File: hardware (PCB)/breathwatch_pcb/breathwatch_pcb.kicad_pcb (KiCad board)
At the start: 2 copper layers, 41.5 x 40.5 mm, 8 parts, among them J1 Conn_01x08_Socket, J2 Conn_01x08_Socket, J4 Conn_01x08_Socket, J5 USB_C_Receptacle_PowerOnly_6P, Q1 AO3401A, SW1 SW_Push

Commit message: changed a bit
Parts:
- R1, R2: footprint Resistor_THT:R_Axial_DIN0207_L6.3mm_D2.5mm_P7.62mm_Horizontal -> Resistor_SMD:R_0603_1608Metric
- moved R2 7.24 mm to (98.5, 68.4)
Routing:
- net Net-(J4-Pin_2): track 22.4 -> 30.0 mm
- net Net-(J2-Pin_2): track 10.6 -> 17.4 mm
- net Net-(J1-Pin_4): track 20.8 -> 27.3 mm
- net GND: track 67.6 -> 70.5 mm
- net Net-(Q1-G): track 14.7 -> 12.8 mm
- net Net-(J1-Pin_3): track 27.9 -> 26.3 mm
- net Net-(J1-Pin_8): track 41.2 -> 42.2 mm
- net Net-(J2-Pin_1): track 15.9 -> 16.9 mm

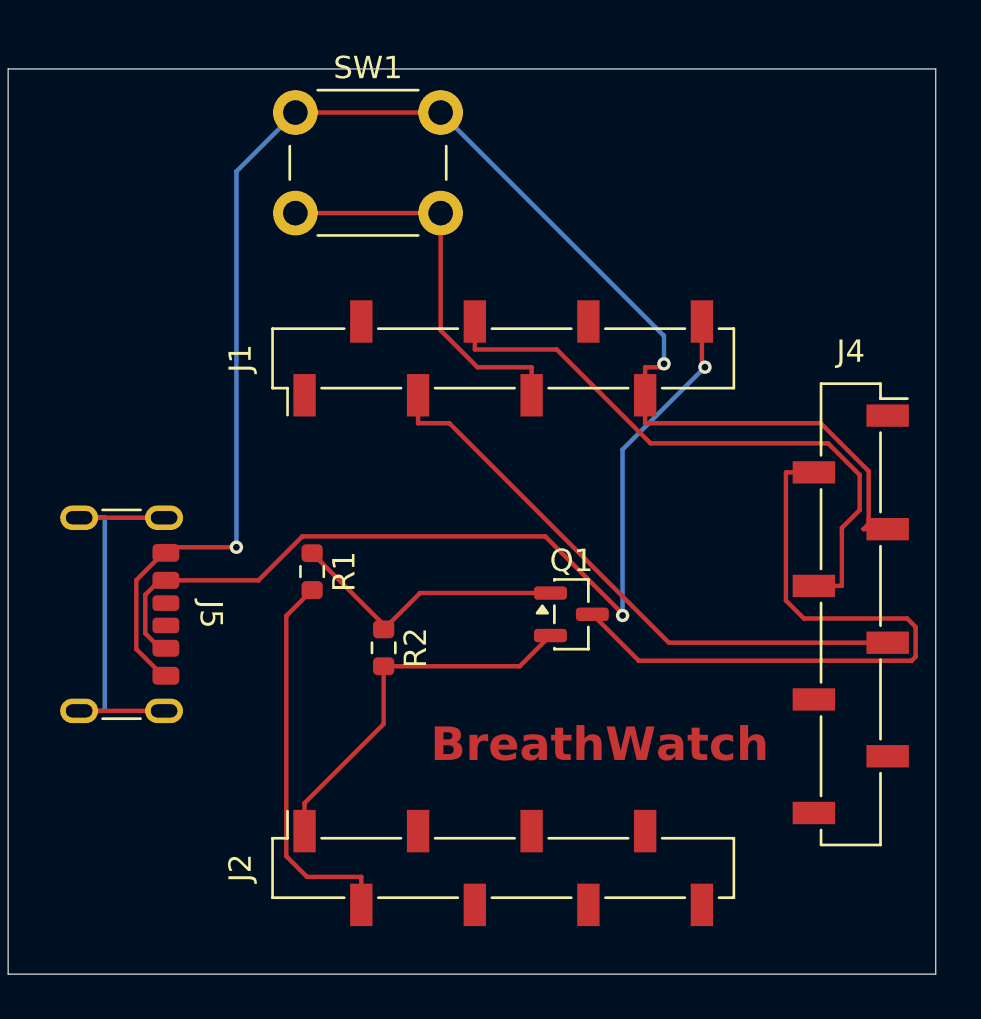
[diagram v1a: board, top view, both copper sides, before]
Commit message: added sensor reading + writing, changed a bit (PCB)
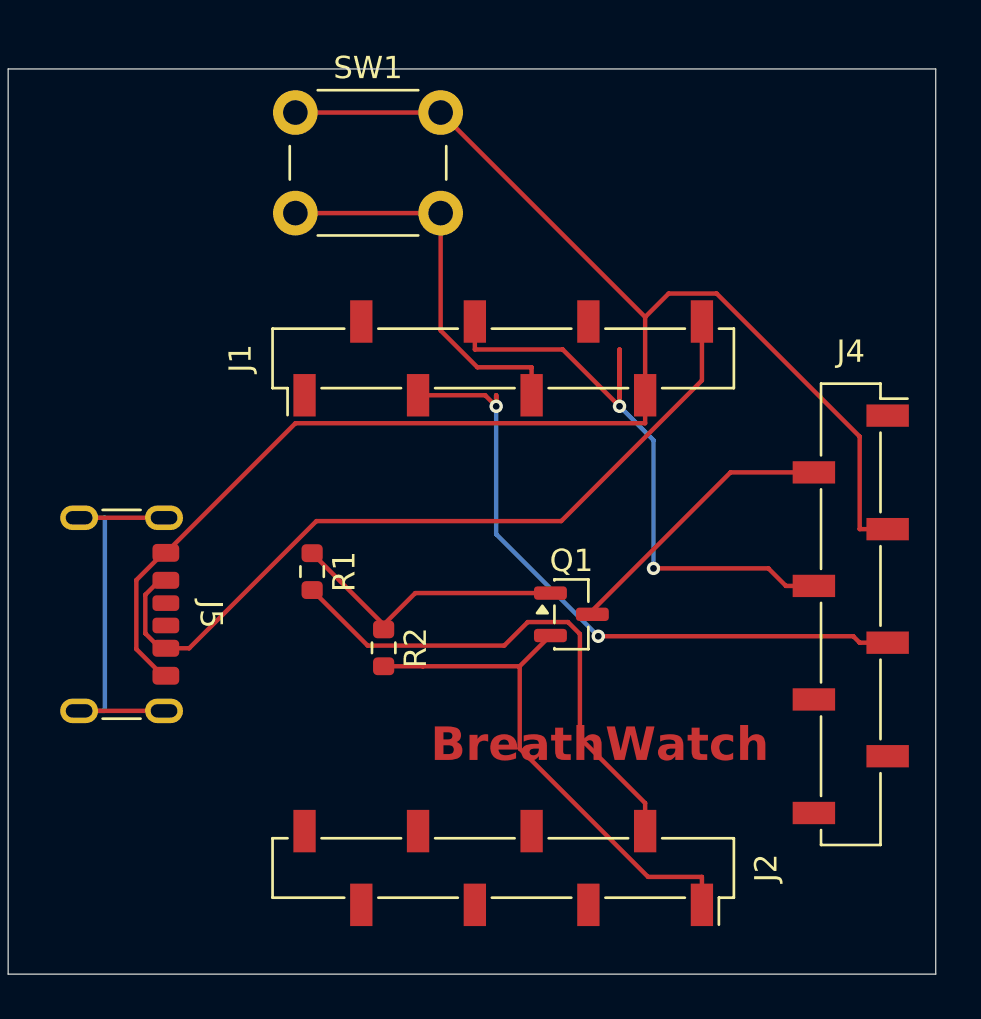
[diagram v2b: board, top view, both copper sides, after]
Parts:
- turned J2 to -90 degrees
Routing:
- net Net-(J4-Pin_2): track 30.0 -> 12.6 mm
- net Net-(J1-Pin_4): track 27.3 -> 34.3 mm, vias 0 -> 2
- net Net-(J2-Pin_1): track 16.9 -> 23.5 mm
- net Net-(J1-Pin_8): track 42.2 -> 35.7 mm, vias 2 -> 0
- net Net-(J2-Pin_2): track 17.4 -> 23.7 mm
- net Net-(J1-Pin_3): track 26.3 -> 30.9 mm, vias 0 -> 2
- net GND: track 70.5 -> 72.8 mm, vias 2 -> 0

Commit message: PCB Design
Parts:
- removed J5: USB_C_Receptacle_PowerOnly_6P, Connector_USB:USB_C_Receptacle_GCT_USB4125-xx-x_6P_TopMnt_Horizontal
- added D1: LED, LED_THT:LED_D5.0mm, F.Cu at (59.3, 67.8)
- added J3: Conn_01x06_Socket, Connector_PinSocket_2.54mm:PinSocket_1x06_P2.54mm_Vertical, F.Cu at (83.6, 71.4)
- added R3: 4.7k, Resistor_SMD:R_0815_2038Metric, F.Cu at (97.4, 89.4)
- added R4: 4.7k, Resistor_SMD:R_0815_2038Metric, F.Cu at (96.5, 94.6)
- added R5: 100k, Resistor_SMD:R_0815_2038Metric, F.Cu at (57.9, 78.9)
- added R6: 330, Resistor_SMD:R_0815_2038Metric, F.Cu at (68.7, 78.7)
- added R7: 4.7k, Resistor_SMD:R_0815_2038Metric, F.Cu at (70.5, 90.2)
- added R8: 330, Resistor_SMD:R_0815_2038Metric, F.Cu at (74.4, 78.7)
- J1: value Conn_01x08_Socket -> Conn_01x20_Socket; footprint Connector_PinSocket_2.54mm:PinSocket_1x08_P2.54mm_Vertical_SMD_Pin1Left -> Connector_PinSocket_2.54mm:PinSocket_1x20_P2.54mm_Vertical
- J2: value Conn_01x08_Socket -> Conn_01x20_Socket; footprint Connector_PinSocket_2.54mm:PinSocket_1x08_P2.54mm_Vertical_SMD_Pin1Right -> Connector_PinSocket_2.54mm:PinSocket_1x20_P2.54mm_Vertical
- J4: footprint Connector_PinSocket_2.54mm:PinSocket_1x08_P2.54mm_Vertical_SMD_Pin1Right -> Connector_PinSocket_2.54mm:PinSocket_1x08_P2.54mm_Vertical
- Q1: value AO3401A -> NMOS; footprint Package_TO_SOT_SMD:SOT-23 -> Package_TO_SOT_THT:TO-220-3_Vertical
- R1: value 100 -> 10k; footprint Resistor_SMD:R_0603_1608Metric -> Resistor_SMD:R_0815_2038Metric
- R2: value 100k -> 20k; footprint Resistor_SMD:R_0603_1608Metric -> Resistor_SMD:R_0815_2038Metric
- SW1: value SW_Push -> SW_Push_Dual_x2; footprint Button_Switch_THT:SW_PUSH_6mm_H7.3mm -> Button_Switch_THT:SW_PUSH_6mm_H4.3mm
- moved J1 59.4 mm to (51.4, 83.4)
- moved Q1 46.8 mm to (60.5, 73.2), turned to 180 degrees
- moved R1 44.1 mm to (65.0, 97.0), turned to 90 degrees
- moved R2 41.7 mm to (63.3, 90.9), turned to 0 degrees
- moved J4 37.9 mm to (109.7, 103.6), turned to 180 degrees
- moved SW1 30.6 mm to (90.6, 74.8), turned to 90 degrees
- moved J2 26.4 mm to (99.7, 104.3)
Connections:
- J1 pad 1: unconnected-(J1-Pin_1-Pad1) -> Net-(J1-Pin_1)
- J1 pad 2: unconnected-(J1-Pin_2-Pad2) -> Net-(D1-K)
- J1 pad 3: Net-(J1-Pin_3) -> unconnected-(J1-Pin_3-Pad3)
- J1 pad 4: Net-(J1-Pin_4) -> unconnected-(J1-Pin_4-Pad4)
- J1 pad 5: Net-(J1-Pin_5) -> unconnected-(J1-Pin_5-Pad5)
- J1 pad 7: GND -> unconnected-(J1-Pin_7-Pad7)
- J2 pad 6: unconnected-(J2-Pin_6-Pad6) -> Net-(J2-Pin_6)
- J2 pad 7: unconnected-(J2-Pin_7-Pad7) -> Net-(J2-Pin_7)
- J4 pad 2: Net-(J4-Pin_2) -> Net-(J2-Pin_1)
- J4 pad 3: GND -> Net-(J2-Pin_2)
- J4 pad 4: Net-(J1-Pin_4) -> Net-(J2-Pin_7)
- J4 pad 5: Net-(J1-Pin_3) -> Net-(J2-Pin_6)
- Q1 pad 1: Net-(Q1-G) -> Net-(J3-Pin_4)
- Q1 pad 2: Net-(J2-Pin_1) -> Net-(Q1-G)
- Q1 pad 3: Net-(J4-Pin_2) -> Net-(D1-K)
- R1 pad 1: Net-(Q1-G) -> Net-(J3-Pin_2)
- R1 pad 2: Net-(J2-Pin_2) -> Net-(J2-Pin_15)
- R2 pad 1: Net-(Q1-G) -> Net-(J3-Pin_2)
- R2 pad 2: Net-(J2-Pin_1) -> Net-(J2-Pin_2)
- SW1 pad 1: GND -> Net-(D1-K)
- SW1 pad 2: Net-(J1-Pin_5) -> Net-(J1-Pin_12)
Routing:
- net GND: track 72.8 -> 0.00 mm
- net Net-(D1-K): track 0.00 -> 63.1 mm, vias 0 -> 1
- net Net-(J3-Pin_2): track 0.00 -> 59.2 mm, vias 0 -> 1
- net Net-(J2-Pin_2): track 23.7 -> 77.0 mm
- net Net-(J1-Pin_1): track 0.00 -> 36.2 mm, vias 0 -> 1
- net Net-(J1-Pin_4): track 34.3 -> 0.00 mm, vias 2 -> 0
- net Net-(J2-Pin_6): track 0.00 -> 33.0 mm, vias 0 -> 1
- net Net-(D1-A): track 0.00 -> 32.2 mm
- net Net-(J2-Pin_13): track 0.00 -> 31.4 mm, vias 0 -> 1
- net Net-(J3-Pin_3): track 0.00 -> 31.4 mm, vias 0 -> 1
- net Net-(J1-Pin_3): track 30.9 -> 0.00 mm, vias 2 -> 0
- net Net-(J2-Pin_7): track 0.00 -> 30.6 mm
- net Net-(J1-Pin_8): track 35.7 -> 7.99 mm
- net Net-(J1-Pin_12): track 0.00 -> 25.8 mm
- net unconnected-(J5-SHIELD-PadS1): track 18.5 -> 0.00 mm
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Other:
- board size 41.5 x 40.5 mm -> 66.3 x 43.7 mm
- board text removed: "BreathWatch"
